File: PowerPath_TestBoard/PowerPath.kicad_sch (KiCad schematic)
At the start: 44 parts, among them J1 24V Test, J2 +24V_Ext, J4 12V Test, J5 5V Test, J6 3V Test, J7 +V_in_24V, J8 GND, J9 +Vin_5V

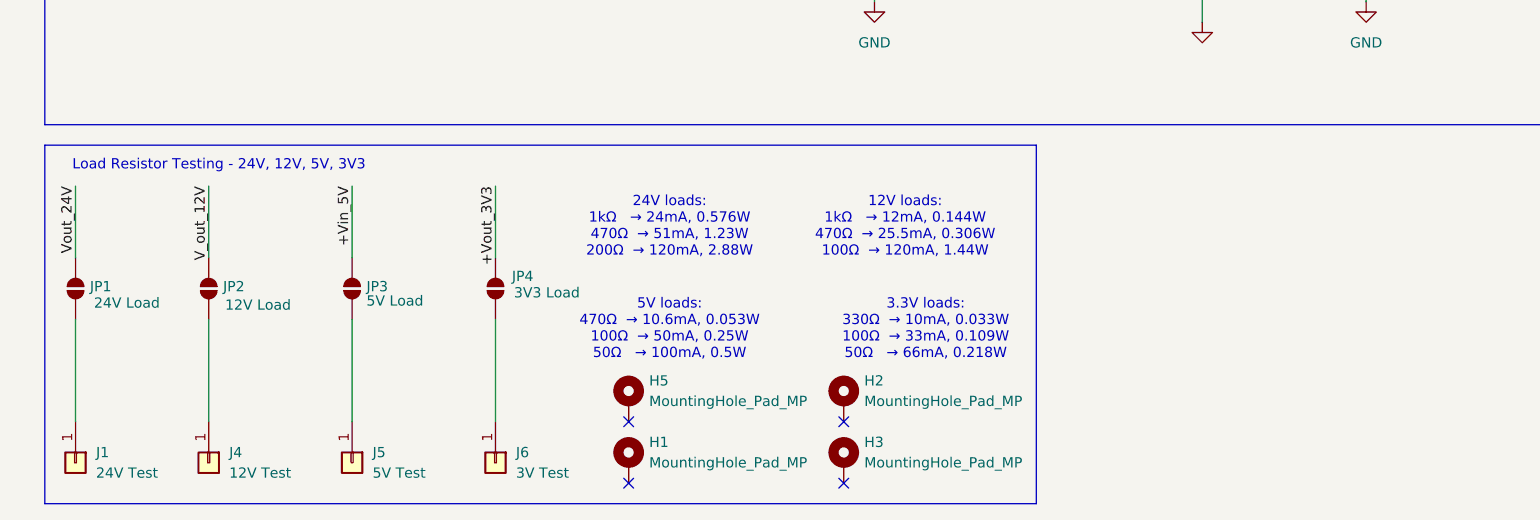
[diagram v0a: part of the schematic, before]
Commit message: added shorting jumpers
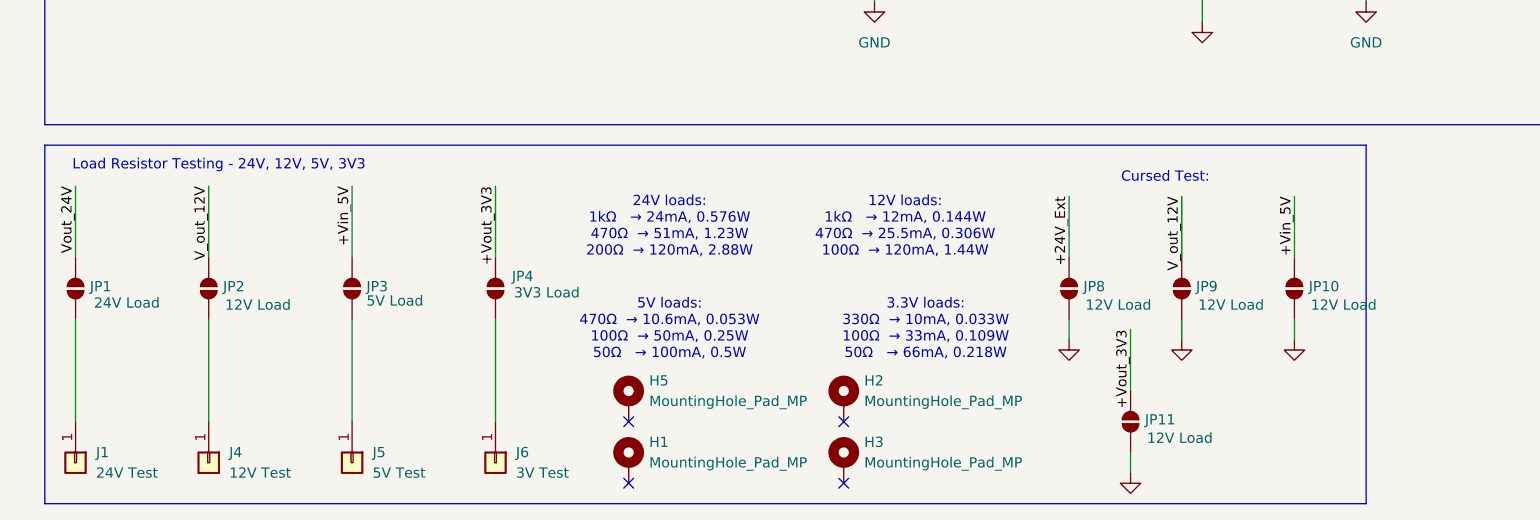
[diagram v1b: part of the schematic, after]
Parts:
- added JP10, JP11, JP8, JP9: 12V Load, Connector_PinHeader_2.54mm:PinHeader_1x02_P2.54mm_Vertical, symbol Jumper:SolderJumper_2_Open
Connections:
- net +24V_Ext: now also JP8.2 (B)
- net +Vin_5V: now also JP10.2 (B)
- net +Vout_3V3: now also JP11.2 (B)
- net GND: now also JP10.1 (A), JP11.1 (A), JP8.1 (A), JP9.1 (A)
- net V_out_12V: now also JP9.2 (B)
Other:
- note added: "Cursed Test:"
